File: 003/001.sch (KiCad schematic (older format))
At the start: 20 parts, among them J1 CONN_01X08, J17 Conn_01x14, J18 Conn_01x14, J2 CONN_01X08

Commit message: Updates
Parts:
- added U1: 2019.All.Mask.02, symbol ArduinoBadge:2019.All.Mask.02
- added U10: Holder.Cu.Mask.01, symbol ArduinoBadge:Holder.Cu.Mask.01
- added U11: logo.B.Mask.Der.01, symbol ArduinoBadge:logo.B.Mask.Der.01
- added U12: logo.B.Mask.Izq.01, symbol ArduinoBadge:logo.B.Mask.Izq.01
- added U13: logo.F.Mask.Der.01, symbol ArduinoBadge:logo.F.Mask.Der.01
- added U14: logo.F.Mask.Izq.01, symbol ArduinoBadge:logo.F.Mask.Izq.01
- added U2: 2019.All.Mask.03, symbol ArduinoBadge:2019.All.Mask.03
- added U3: Arduino.SilkS, symbol ArduinoBadge:Arduino.SilkS
- added U4: Edge.Back.Only.SilkS.02, symbol ArduinoBadge:Edge.Back.Only.SilkS.02
- added U5: Edge.Only.SilkS.02, symbol ArduinoBadge:Edge.Only.SilkS.02
- added U6: Fig.04.Cu.Mask, symbol ArduinoBadge:Fig.04.Cu.Mask
- added U7: Fig.05.Cu.Mask, symbol ArduinoBadge:Fig.05.Cu.Mask
- added U8: Fig.06.Cu.Mask, symbol ArduinoBadge:Fig.06.Cu.Mask
- added U9: Holder.B.Cu.Mask.01, symbol ArduinoBadge:Holder.B.Cu.Mask.01
- J1, J2: footprint (none) -> Connector_PinSocket_2.54mm:PinSocket_1x08_P2.54mm_Vertical_SMD_Pin1Left
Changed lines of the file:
@@
 F 0 "J1" H 5150 4725 50  0000 L CNN
 F 1 "CONN_01X08" H 4950 4625 50  0000 L CNN
-F 2 "" H 5200 4150 50  0001 C CNN
+F 2 "Connector_PinSocket_2.54mm:PinSocket_1x08_P2.54mm_Vertical_SMD_Pin1Left" H 5200 4150 50  0001 C CNN
 F 3 "" H 5200 4150 50  0001 C CNN
 	1    5200 4150
@@
 F 0 "J2" H 5717 4715 50  0000 C CNN
 F 1 "CONN_01X08" H 5717 4624 50  0000 C CNN
-F 2 "" H 5800 4150 50  0001 C CNN
+F 2 "Connector_PinSocket_2.54mm:PinSocket_1x08_P2.54mm_Vertical_SMD_Pin1Left" H 5800 4150 50  0001 C CNN
 F 3 "" H 5800 4150 50  0001 C CNN
 	1    5800 4150
@@
 	1    0    0    -1
 $EndComp
+$Comp
+L ArduinoBadge:2019.All.Mask.02 U1
+U 1 1 5C5C8D11
+P 1000 5250
+F 0 "U1" H 1140 5296 50  0000 L CNN
+F 1 "2019.All.Mask.02" H 1140 5205 50  0000 L CNN
+F 2 "" H 1000 5250 50  0001 C CNN
+F 3 "" H 1000 5250 50  0001 C CNN
+	1    1000 5250
+	1    0    0    -1
+$EndComp
+$Comp
+L ArduinoBadge:2019.All.Mask.03 U2
+U 1 1 5C5C9718
+P 1000 5525
+F 0 "U2" H 1140 5571 50  0000 L CNN
+F 1 "2019.All.Mask.03" H 1140 5480 50  0000 L CNN
+F 2 "" H 1000 5525 50  0001 C CNN
+F 3 "" H 1000 5525 50  0001 C CNN
+	1    1000 5525
+	1    0    0    -1
+$EndComp
+$Comp
+L ArduinoBadge:Arduino.SilkS U3
+U 1 1 5C5C9FC2
+P 1000 5825
+F 0 "U3" H 1140 5871 50  0000 L CNN
+F 1 "Arduino.SilkS" H 1140 5780 50  0000 L CNN
+F 2 "" H 1000 5825 50  0001 C CNN
+F 3 "" H 1000 5825 50  0001 C CNN
+	1    1000 5825
+	1    0    0    -1
+$EndComp
+$Comp
+L ArduinoBadge:Edge.Back.Only.SilkS.02 U4
+U 1 1 5C5CA837
+P 1000 6125
+F 0 "U4" H 1140 6171 50  0000 L CNN
+F 1 "Edge.Back.Only.SilkS.02" H 1140 6080 50  0000 L CNN
+F 2 "" H 1000 6125 50  0001 C CNN
+F 3 "" H 1000 6125 50  0001 C CNN
+	1    1000 6125
+	1    0    0    -1
+$EndComp
+$Comp
+L ArduinoBadge:Edge.Only.SilkS.02 U5
+U 1 1 5C5CB3CB
+P 1000 6425
+F 0 "U5" H 1140 6471 50  0000 L CNN
+F 1 "Edge.Only.SilkS.02" H 1140 6380 50  0000 L CNN
+F 2 "" H 1000 6425 50  0001 C CNN
+F 3 "" H 1000 6425 50  0001 C CNN
+	1    1000 6425
+	1    0    0    -1
+$EndComp
+$Comp
+L ArduinoBadge:Fig.04.Cu.Mask U6
+U 1 1 5C5CBB6E
+P 1000 6725
+F 0 "U6" H 1140 6771 50  0000 L CNN
+F 1 "Fig.04.Cu.Mask" H 1140 6680 50  0000 L CNN
+F 2 "" H 1000 6725 50  0001 C CNN
+F 3 "" H 1000 6725 50  0001 C CNN
+	1    1000 6725
+	1    0    0    -1
+$EndComp
+$Comp
+L ArduinoBadge:Fig.05.Cu.Mask U7
+U 1 1 5C5CC4BE
+P 1000 7050
+F 0 "U7" H 1140 7096 50  0000 L CNN
+F 1 "Fig.05.Cu.Mask" H 1140 7005 50  0000 L CNN
+F 2 "" H 1000 7050 50  0001 C CNN
+F 3 "" H 1000 7050 50  0001 C CNN
+	1    1000 7050
+	1    0    0    -1
+$EndComp
+$Comp
+L ArduinoBadge:Fig.06.Cu.Mask U8
+U 1 1 5C5CCA64
+P 2500 5250
+F 0 "U8" H 2640 5296 50  0000 L CNN
+F 1 "Fig.06.Cu.Mask" H 2640 5205 50  0000 L CNN
+F 2 "" H 2500 5250 50  0001 C CNN
+F 3 "" H 2500 5250 50  0001 C CNN
+	1    2500 5250
+	1    0    0    -1
+$EndComp
+$Comp
+L ArduinoBadge:Holder.B.Cu.Mask.01 U9
+U 1 1 5C5CCEC9
+P 2500 5550
+F 0 "U9" H 2640 5596 50  0000 L CNN
+F 1 "Holder.B.Cu.Mask.01" H 2640 5505 50  0000 L CNN
+F 2 "" H 2500 5550 50  0001 C CNN
+F 3 "" H 2500 5550 50  0001 C CNN
+	1    2500 5550
+	1    0    0    -1
+$EndComp
+$Comp
+L ArduinoBadge:Holder.Cu.Mask.01 U10
+U 1 1 5C5CD33A
+P 2500 5850
+F 0 "U10" H 2640 5896 50  0000 L CNN
+F 1 "Holder.Cu.Mask.01" H 2640 5805 50  0000 L CNN
+F 2 "" H 2500 5850 50  0001 C CNN
+F 3 "" H 2500 5850 50  0001 C CNN
+	1    2500 5850
+	1    0    0    -1
+$EndComp
+$Comp
+L ArduinoBadge:logo.B.Mask.Der.01 U11
+U 1 1 5C5CD7B7
+P 2500 6175
+F 0 "U11" H 2640 6221 50  0000 L CNN
+F 1 "logo.B.Mask.Der.01" H 2640 6130 50  0000 L CNN
+F 2 "" H 2500 6175 50  0001 C CNN
+F 3 "" H 2500 6175 50  0001 C CNN
+	1    2500 6175
+	1    0    0    -1
+$EndComp
+$Comp
+L ArduinoBadge:logo.B.Mask.Izq.01 U12
+U 1 1 5C5CDC40
+P 2500 6475
+F 0 "U12" H 2640 6521 50  0000 L CNN
+F 1 "logo.B.Mask.Izq.01" H 2640 6430 50  0000 L CNN
+F 2 "" H 2500 6475 50  0001 C CNN
+F 3 "" H 2500 6475 50  0001 C CNN
+	1    2500 6475
+	1    0    0    -1
+$EndComp
+$Comp
+L ArduinoBadge:logo.F.Mask.Der.01 U13
+U 1 1 5C5CE0D5
+P 2500 6775
+F 0 "U13" H 2640 6821 50  0000 L CNN
+F 1 "logo.F.Mask.Der.01" H 2640 6730 50  0000 L CNN
+F 2 "" H 2500 6775 50  0001 C CNN
+F 3 "" H 2500 6775 50  0001 C CNN
+	1    2500 6775
+	1    0    0    -1
+$EndComp
+$Comp
+L ArduinoBadge:logo.F.Mask.Izq.01 U14
+U 1 1 5C5CE576
+P 2500 7050
+F 0 "U14" H 2640 7096 50  0000 L CNN
+F 1 "logo.F.Mask.Izq.01" H 2640 7005 50  0000 L CNN
+F 2 "" H 2500 7050 50  0001 C CNN
+F 3 "" H 2500 7050 50  0001 C CNN
+	1    2500 7050
+	1    0    0    -1
+$EndComp

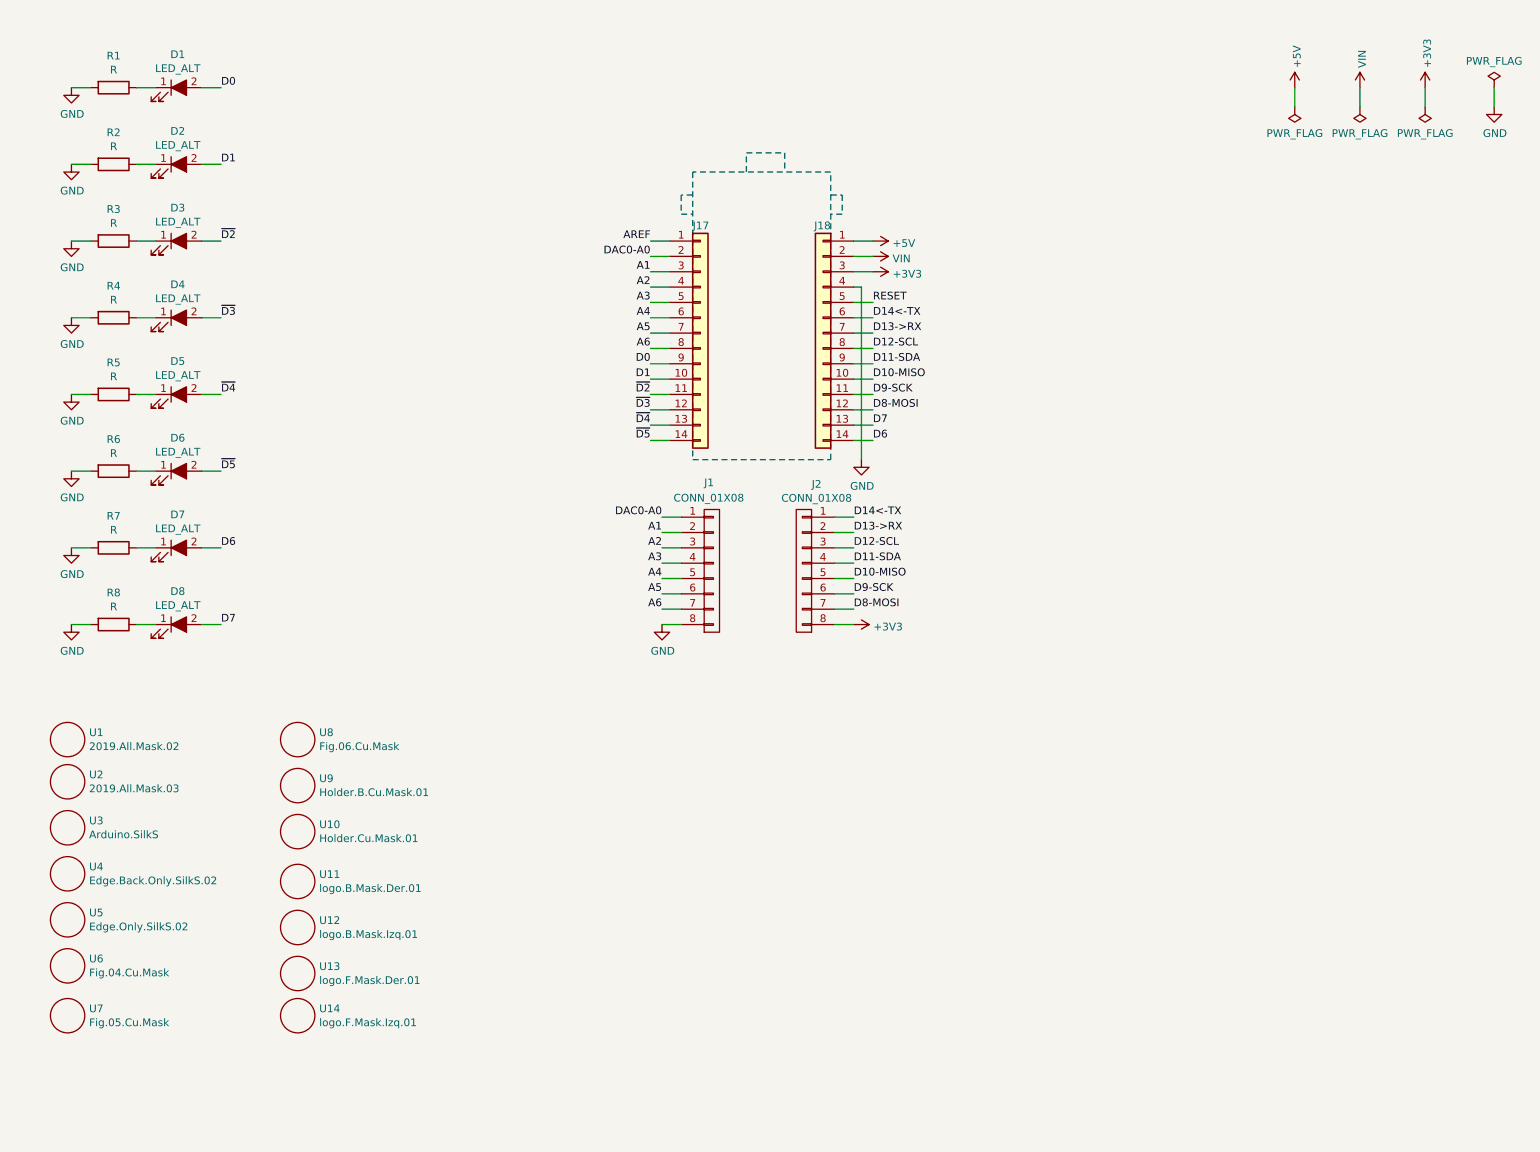
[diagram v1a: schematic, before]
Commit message: Add Footprint MKR Family
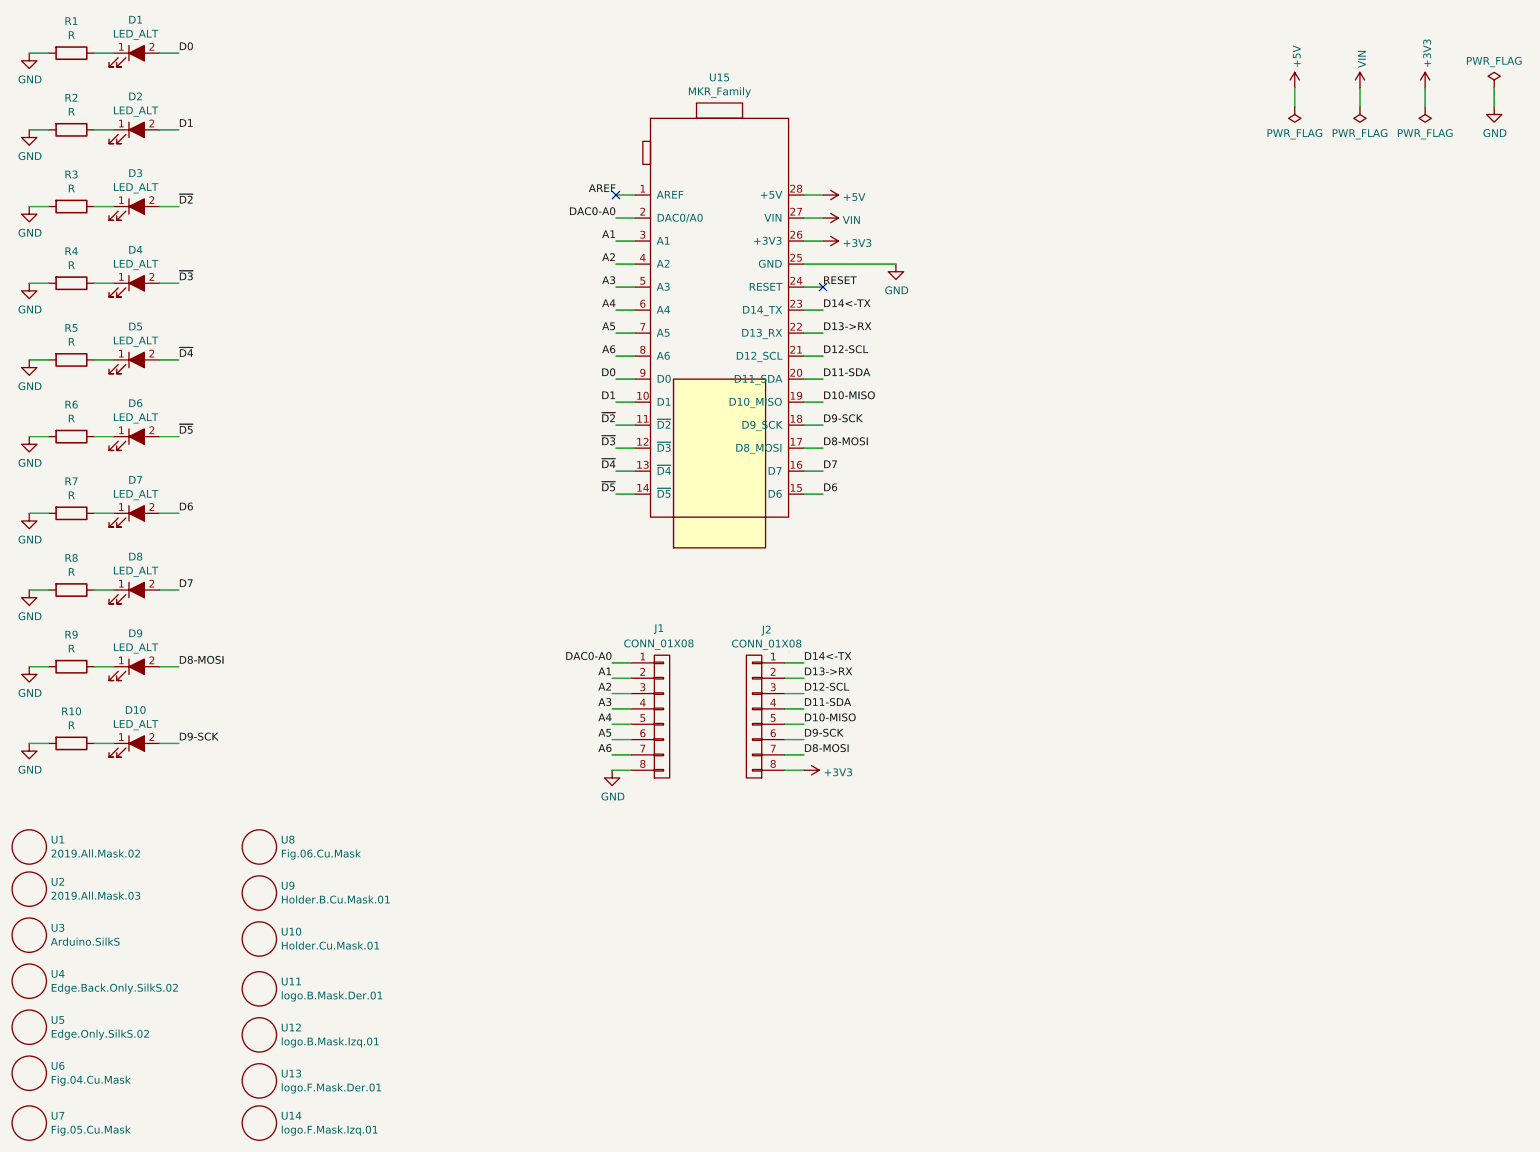
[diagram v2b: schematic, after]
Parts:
- removed J17, J18: Conn_01x14, Connector_PinSocket_2.54mm:PinSocket_1x14_P2.54mm_Vertical_SMD_Pin1Left, symbol 001-rescue:Conn_01x14-Connector_Generic
- added D10, D9: LED_ALT, ArduinoBadge:SunLed_PLCC_Reverse-2, symbol device:LED_ALT
- added R10, R9: R, Resistor_SMD:R_1206_3216Metric_Pad1.39x1.80mm_HandSolder, symbol device:R
- added U15: MKR_Family, ArduinoBadge:MKR_Family_SMD, symbol ArduinoBadge:MKR_Family
- U1: footprint (none) -> ArduinoBadge:2019.All.Mask.02
- U10: footprint (none) -> ArduinoBadge:Holder.Cu.Mask.01
- U11: footprint (none) -> ArduinoBadge:logo.B.Mask.Der.01
- U12: footprint (none) -> ArduinoBadge:logo.B.Mask.Izq.01
- U13: footprint (none) -> ArduinoBadge:logo.F.Mask.Der.01
- U14: footprint (none) -> ArduinoBadge:logo.F.Mask.Izq.01
- U2: footprint (none) -> ArduinoBadge:2019.All.Mask.03
- U3: footprint (none) -> ArduinoBadge:Arduino.SilkS
- U4: footprint (none) -> ArduinoBadge:Edge.Back.Only.SilkS.02
- U5: footprint (none) -> ArduinoBadge:Edge.Only.SilkS.02
- U6: footprint (none) -> ArduinoBadge:Fig.04.Cu.Mask
- U7: footprint (none) -> ArduinoBadge:Fig.05.Cu.Mask
- U8: footprint (none) -> ArduinoBadge:Fig.06.Cu.Mask
- U9: footprint (none) -> ArduinoBadge:Holder.B.Cu.Mask.01
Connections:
- net +3V3: now also U15.26 (+3V3)
- net +5V: now also U15.28 (+5V)
- net A1: now also U15.3 (A1)
- net A2: now also U15.4 (A2)
- net A3: now also U15.5 (A3)
- net A4: now also U15.6 (A4)
- net A5: now also U15.7 (A5)
- net A6: now also U15.8 (A6)
- net AREF: now also U15.1 (AREF)
- net D0: now also U15.9 (D0)
- net D1: now also U15.10 (D1)
- net D10-MISO: now also U15.19 (D10_MISO)
- net D11-SDA: now also U15.20 (D11_SDA)
- net D12-SCL: now also U15.21 (D12_SCL)
- net D13->RX: now also U15.22 (D13_RX)
- net D14<-TX: now also U15.23 (D14_TX)
- net D6: now also U15.15 (D6)
- net D7: now also U15.16 (D7)
- net D8-MOSI: now also D9.2 (A), U15.17 (D8_MOSI)
- net D9-SCK: now also D10.2 (A), U15.18 (D9_SCK)
- net DAC0-A0: now also U15.2 (DAC0/A0)
- net GND: now also R10.2, R9.2, U15.25 (GND)
- net RESET: now also U15.24 (RESET)
- net VIN: now also U15.27 (VIN)
- net ~D2: now also U15.11 (~D2)
- net ~D3: now also U15.12 (~D3)
- net ~D4: now also U15.13 (~D4)
- net ~D5: now also U15.14 (~D5)
- new net: D9.1 (K), R9.1
- new net: D10.1 (K), R10.1
- no-connect marks 0 -> 2
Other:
- moved on the sheet: D1, D2, D3, D4, D5, D6, D7, D8, J1, J2, R1, R2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
